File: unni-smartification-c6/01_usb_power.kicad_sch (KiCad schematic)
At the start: 36 parts, among them J1 USB-C (replacement daughterbo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, J2 Li-Ion 1S JST-PH, J4 UNNI DC / battery input - AC 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, Q1 AO3401A, Q2 AO3401A, Q3 AO3400A, Q4 AO3400A, U1 MCP73831T-2ACI/OT, U2 TPS63031DSK, U3 TPS613222ADBZ (5V)

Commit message: trying routing the usb-pcb
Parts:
- added U4: USBLC6-2SC6, Package_TO_SOT_SMD:SOT-23-6, symbol Power_Protection:USBLC6-2SC6
- D1, D3, D4: footprint Diode_SMD:D_SMA -> Diode_SMD:D_SMA_Handsoldering
- Q1, Q2, Q3, Q4, U3: footprint Package_TO_SOT_SMD:SOT-23 -> Package_TO_SOT_SMD:SOT-23_Handsoldering
- U1: footprint Package_TO_SOT_SMD:SOT-23-5 -> Package_TO_SOT_SMD:SOT-23-5_HandSoldering
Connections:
- net +BATT: now also J2.2 (Pin_2); no longer J2.1 (Pin_1)
- net GND: now also J2.1 (Pin_1), U4.2 (GND); no longer J2.2 (Pin_2)
- net USB_RAW_N: now also U4.6 (I/O1); no longer J1.A7 (DN1), J1.B7 (DN2)
- net USB_RAW_P: now also U4.4 (I/O2); no longer J1.A6 (DP1), J1.B6 (DP2)
- net VBUS: now also U4.5 (VBUS)
- new net USB_N: J1.A7 (DN1), J1.B7 (DN2), U4.1 (I/O1)
- new net USB_P: J1.A6 (DP1), J1.B6 (DP2), U4.3 (I/O2)

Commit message: add usb-esp and finalize usb-pcb
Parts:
- added C14: 100n, Capacitor_SMD:C_0603_1608Metric_Pad1.08x0.95mm_HandSolder, symbol Device:C
- L1: value 1.5uH -> 2.2uH
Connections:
- net GND: now also C14.2
- net VBUS: now also C14.1
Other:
- moved on the sheet: R1
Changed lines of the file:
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@@
 	)
 	(junction
+		(at 66.04 46.99)
+		(diameter 0)
+		(color 0 0 0 0)
+	)
+	(junction
 		(at 66.04 53.34)
 		(diameter 0)
@@
 	)
 	(junction
+		(at 66.04 30.48)
+		(diameter 0)
+		(color 0 0 0 0)
+	)
+	(junction
 		(at 49.53 73.66)
 		(diameter 0)
@@
 	(wire
 		(pts
+			(xy 66.04 30.48) (xy 90.17 30.48)
+		)
+		(stroke
+			(width 0)
+			(type default)
+		)
+	)
+	(wire
+		(pts
 			(xy 39.37 172.72) (xy 39.37 193.04)
 		)
@@
 	(wire
 		(pts
-			(xy 45.72 53.34) (xy 50.8 53.34)
+			(xy 45.72 53.34) (xy 52.07 53.34)
 		)
 		(stroke
@@
 	(wire
 		(pts
+			(xy 66.04 46.99) (xy 66.04 53.34)
+		)
+		(stroke
+			(width 0)
+			(type default)
+		)
+	)
+	(wire
+		(pts
 			(xy 137.16 31.75) (xy 137.16 30.48)
 		)
@@
 	(wire
 		(pts
+			(xy 66.04 46.99) (xy 90.17 46.99)
+		)
+		(stroke
+			(width 0)
+			(type default)
+		)
+	)
+	(wire
+		(pts
 			(xy 45.72 33.02) (xy 50.8 33.02)
 		)
@@
 	(wire
 		(pts
+			(xy 90.17 30.48) (xy 90.17 34.29)
+		)
+		(stroke
+			(width 0)
+			(type default)
+		)
+	)
+	(wire
+		(pts
 			(xy 133.35 189.23) (xy 133.35 191.77)
 		)
@@
 	(wire
 		(pts
-			(xy 66.04 45.72) (xy 66.04 53.34)
+			(xy 66.04 45.72) (xy 66.04 46.99)
 		)
 		(stroke
@@
 	(wire
 		(pts
-			(xy 58.42 53.34) (xy 66.04 53.34)
+			(xy 59.69 53.34) (xy 66.04 53.34)
 		)
 		(stroke
@@
 	(wire
 		(pts
+			(xy 90.17 41.91) (xy 90.17 46.99)
+		)
+		(stroke
+			(width 0)
+			(type default)
+		)
+	)
+	(wire
+		(pts
 			(xy 123.19 39.37) (xy 123.19 54.61)
 		)
@@
 	(symbol
 		(lib_id "Device:R")
-		(at 54.61 53.34 90)
+		(at 55.88 53.34 90)
 		(unit 1)
 		(body_style 1)
@@
 		(fields_autoplaced yes)
 		(property "Reference" "R1"
-			(at 54.61 46.99 90)
+			(at 55.88 46.99 90)
 			(show_name no)
 			(do_not_autoplace no)
@@
 		)
 		(property "Value" "5.1k"
-			(at 54.61 49.53 90)
+			(at 55.88 49.53 90)
 			(show_name no)
 			(do_not_autoplace no)
@@
 		)
 		(property "Footprint" "Resistor_SMD:R_0805_2012Metric_Pad1.20x1.40mm_HandSolder"
-			(at 54.61 53.34 0)
+			(at 55.88 53.34 0)
 			(hide yes)
 			(show_name no)
@@
 		)
 		(property "Datasheet" ""
-			(at 54.61 53.34 0)
+			(at 55.88 53.34 0)
 			(hide yes)
 			(show_name no)
@@
 		)
 		(property "Description" ""
-			(at 54.61 53.34 0)
+			(at 55.88 53.34 0)
 			(hide yes)
 			(show_name no)
@@
 			)
 		)
-		(property "Value" "1.5uH"
+		(property "Value" "2.2uH"
 			(at 186.69 130.81 0)
 			(show_name no)
@@
 	)
 	(symbol
+		(lib_id "Device:C")
+		(at 90.17 38.1 0)
+		(unit 1)
+		(body_style 1)
+		(exclude_from_sim yes)
+		(in_bom yes)
+		(on_board yes)
+		(in_pos_files yes)
+		(dnp no)
+		(fields_autoplaced yes)
+		(property "Reference" "C14"
+			(at 93.98 36.8299 0)
+			(show_name no)
+			(do_not_autoplace no)
+			(effects
+				(font
+					(size 1.27 1.27)
+				)
+				(justify left)
+			)
+		)
+		(property "Value" "100n"
+			(at 93.98 39.3699 0)
+			(show_name no)
+			(do_not_autoplace no)
+			(effects
+				(font
+					(size 1.27 1.27)
+				)
+				(justify left)
+			)
+		)
+		(property "Footprint" "Capacitor_SMD:C_0603_1608Metric_Pad1.08x0.95mm_HandSolder"
+			(at 91.1352 41.91 0)
+			(hide yes)
+			(show_name no)
+			(do_not_autoplace no)
+			(effects
+				(font
+					(size 1.27 1.27)
+				)
+			)
+		)
+		(property "Datasheet" ""
+			(at 90.17 38.1 0)
+			(hide yes)
+			(show_name no)
+			(do_not_autoplace no)
+			(effects
+				(font
+					(size 1.27 1.27)
+				)
+			)
+		)
+		(property "Description" "Unpolarized capacitor"
+			(at 90.17 38.1 0)
+			(hide yes)
+			(show_name no)
+			(do_not_autoplace no)
+			(effects
+				(font
+					(size 1.27 1.27)
+				)
+			)
+		)
+		(pin "1"
+		)
+		(pin "2"
+		)
+		(instances
+			(project "unni-smartification-c6"
+				(path "/15fd0edf-be3e-44ec-8dd6-6b1cf69b7c51/c2ff28aa-a0f2-4a89-9a60-62d08b111b12"
+					(reference "C14")
+					(unit 1)
+				)
+			)
+		)
+	)
+	(symbol
 		(lib_id "power:+5V")
 		(at 227.33 168.91 0)
@@
 		(unit 1)
 		(body_style 1)
-		(exclude_from_sim no)
+		(exclude_from_sim yes)
 		(in_bom yes)
 		(on_board yes)
@@
 		)
 		(property "Value" "VBUS"
-			(at 50.8 22.86 0)
+			(at 53.34 26.67 0)
 			(show_name no)
 			(do_not_autoplace no)
@@
 					(size 1 1)
 				)
+				(justify left)
 			)
 		)
@@
 		)
 		(property "Value" "GND"
-			(at 66.04 88.9 0)
+			(at 68.58 85.09 0)
 			(show_name no)
 			(do_not_autoplace no)
@@
 					(size 1 1)
 				)
+				(justify left)
 			)
 		)
@@
 		(in_pos_files yes)
 		(dnp no)
+		(fields_autoplaced yes)
 		(property "Reference" "J2"
-			(at 34.29 110.49 0)
+			(at 34.29 95.25 0)
 			(show_name no)
 			(do_not_autoplace no)
@@
 		)
 		(property "Value" "Li-Ion 1S JST-PH"
-			(at 34.29 107.95 0)
+			(at 34.29 97.79 0)
 			(show_name no)
 			(do_not_autoplace no)

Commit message: move some power stuff to esp board, update some footprints
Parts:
- removed C1, C2: 4.7uF, Capacitor_SMD:C_0805_2012Metric_Pad1.18x1.45mm_HandSolder, symbol Device:C
- removed C3, C5, C6: 10uF, Capacitor_SMD:C_0805_2012Metric_Pad1.18x1.45mm_HandSolder, symbol Device:C
- removed C4: 100nF, Capacitor_SMD:C_0603_1608Metric_Pad1.08x0.95mm_HandSolder, symbol Device:C
- removed D1: SS14, Diode_SMD:D_SMA_Handsoldering, symbol Diode:SB120
- removed J2: Li-Ion 1S JST-PH, Connector_JST:JST_PH_S2B-PH-SM4-TB_1x02-1MP_P2.00mm_Horizontal, symbol Connector_Generic:Conn_01x02
- removed L1: 2.2uH, Inductor_SMD:L_TDK_NLV32_3.2x2.5mm, symbol Device:L
- removed Q1: AO3401A, Package_TO_SOT_SMD:SOT-23_Handsoldering, symbol Transistor_FET:TP0610T
- removed R11: 150k, Resistor_SMD:R_0805_2012Metric_Pad1.20x1.40mm_HandSolder, symbol Device:R
- removed R12: 220k, Resistor_SMD:R_0805_2012Metric_Pad1.20x1.40mm_HandSolder, symbol Device:R
- removed R3: 3.3k, Resistor_SMD:R_0805_2012Metric_Pad1.20x1.40mm_HandSolder, symbol Device:R
- removed R5: 100k, Resistor_SMD:R_0805_2012Metric_Pad1.20x1.40mm_HandSolder, symbol Device:R
- removed R6: 1M, Resistor_SMD:R_0805_2012Metric_Pad1.20x1.40mm_HandSolder, symbol Device:R
- removed U1: MCP73831T-2ACI/OT, Package_TO_SOT_SMD:SOT-23-5_HandSoldering, symbol Battery_Management:MCP73831-2-OT
- removed U2: TPS63031DSK, Package_SON:WSON-10-1EP_2.5x2.5mm_P0.5mm_EP1.2x2mm, symbol Regulator_Switching:TPS63030DSK
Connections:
- net GND: now also J4.2 (Pin_2); no longer J4.3 (Pin_3)
- net UNNI_AC: now also J4.3 (Pin_3); no longer J4.2 (Pin_2)
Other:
- note removed: "RPROG 3.3k = ~303 mA nominal charge current"
- moved on the sheet: D3, D4

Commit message: re-do ESP PCB
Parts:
- added J3: Conn_01x01, Connector_Wire:SolderWire-0.5sqmm_1x01_D0.9mm_OD2.1mm, symbol Connector_Generic:Conn_01x01
- added J5, J6, J7, J8, J9: Conn_01x01, Connector_Wire:SolderWire-0.1sqmm_1x01_D0.4mm_OD1mm, symbol Connector_Generic:Conn_01x01
- L2: footprint Inductor_SMD:L_TDK_NLV32_3.2x2.5mm -> Unni_Inductor:L_Murata_DFE322520FD_3.2x2.5mm_HandSolder
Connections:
- net BOOST_CMD: now also J5.1 (Pin_1)
- net USB_N renamed USBPort_N
- net USB_P renamed USBPort_P
- net USB_RAW_N renamed CONN_USB_N
- net CONN_USB_N: now also J9.1 (Pin_1)
- net USB_RAW_P renamed CONN_USB_P
- net CONN_USB_P: now also J8.1 (Pin_1)
- new net CONN_+BATT: J7.1 (Pin_1)
- new net CONN_GND: J3.1 (Pin_1)
- new net CONN_VBUS: J6.1 (Pin_1)

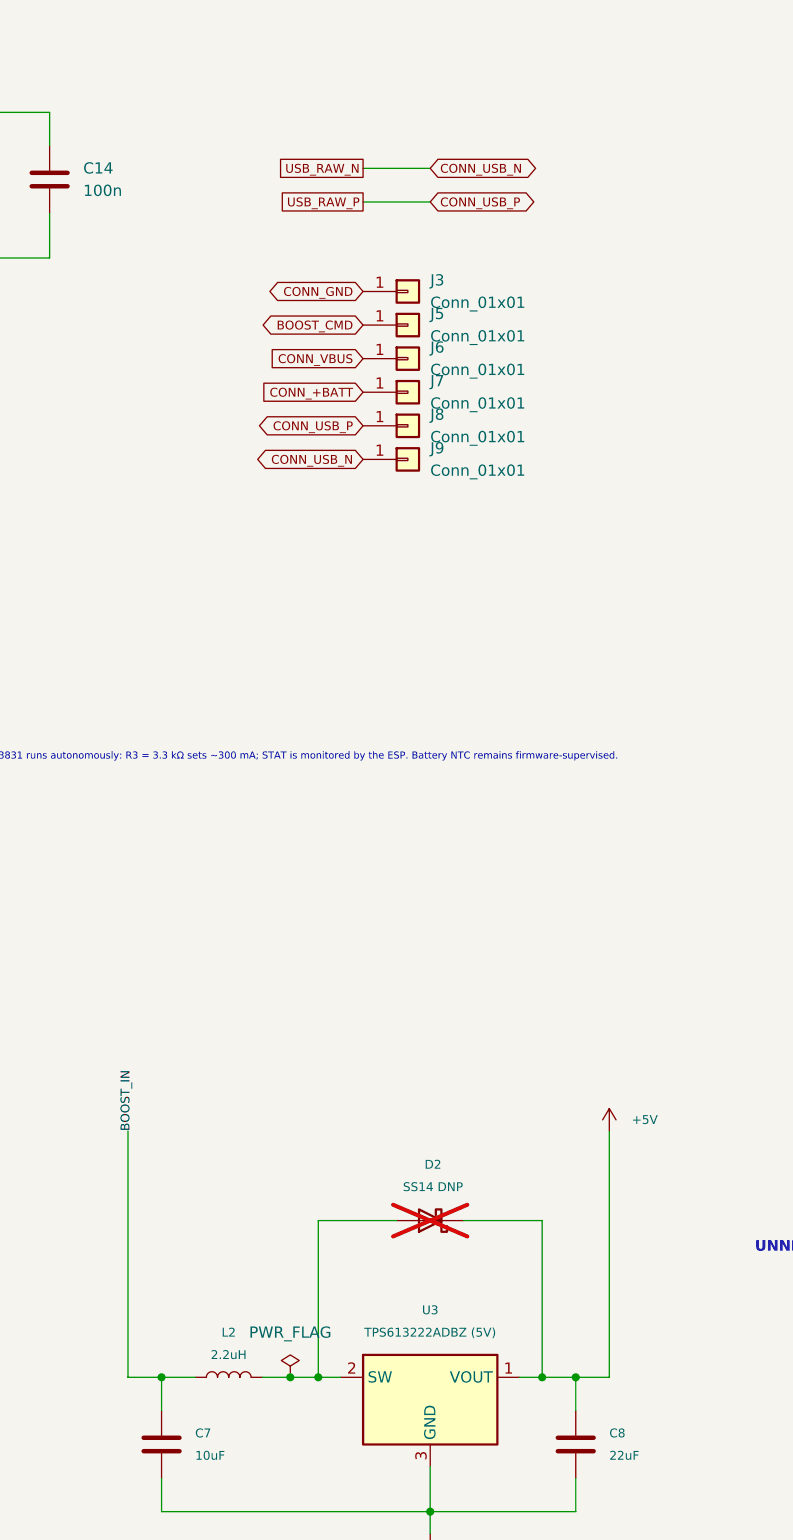
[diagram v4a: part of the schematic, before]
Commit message: Clean up power nets and routing rules
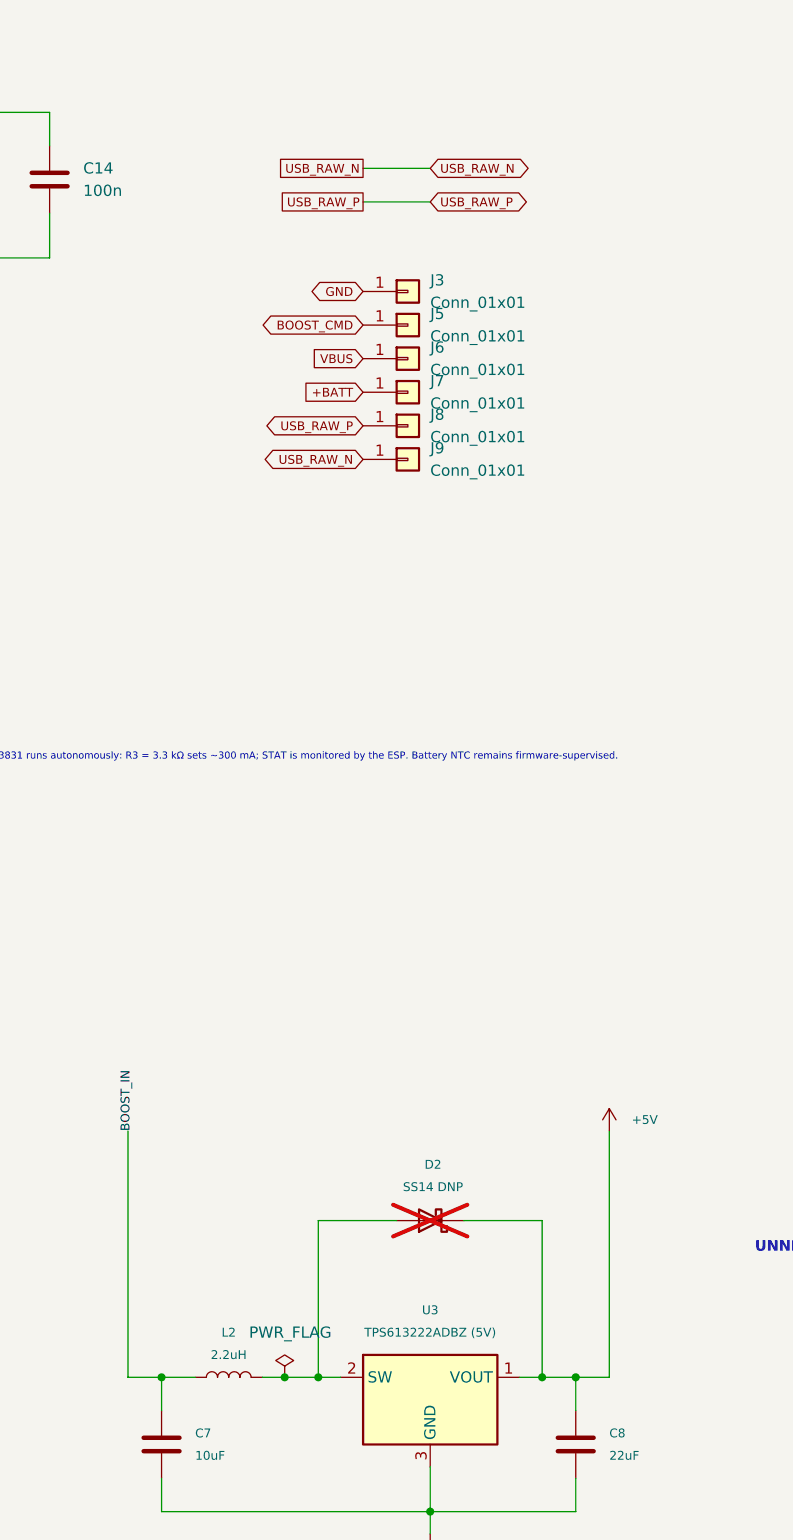
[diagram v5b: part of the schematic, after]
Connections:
- net CONN_+BATT is gone; now on net +BATT: J7.1 (Pin_1)
- net CONN_GND is gone; now on net GND: J3.1 (Pin_1)
- net CONN_VBUS is gone; now on net VBUS: J6.1 (Pin_1)
- net CONN_USB_N renamed USB_RAW_N
- net CONN_USB_P renamed USB_RAW_P
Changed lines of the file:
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@@
 	)
 	(junction
-		(at 117.475 173.99)
+		(at 116.84 173.99)
 		(diameter 0)
 		(color 0 0 0 0)
@@
 	(wire
 		(pts
-			(xy 117.475 173.99) (xy 120.65 173.99)
+			(xy 116.84 173.99) (xy 120.65 173.99)
 		)
 		(stroke
@@
 	(wire
 		(pts
-			(xy 114.3 173.99) (xy 117.475 173.99)
+			(xy 114.3 173.99) (xy 116.84 173.99)
 		)
 		(stroke
@@
 		)
 	)
-	(global_label "CONN_USB_P"
+	(global_label "USB_RAW_P"
 		(shape bidirectional)
 		(at 125.73 66.04 180)
@@
 		)
 	)
-	(global_label "CONN_+BATT"
+	(global_label "+BATT"
 		(shape input)
 		(at 125.73 62.23 180)
@@
 		)
 	)
-	(global_label "CONN_USB_P"
+	(global_label "USB_RAW_P"
 		(shape bidirectional)
 		(at 133.35 40.64 0)
@@
 		)
 	)
-	(global_label "CONN_GND"
+	(global_label "GND"
 		(shape bidirectional)
 		(at 125.73 50.8 180)
@@
 		)
 	)
-	(global_label "CONN_USB_N"
+	(global_label "USB_RAW_N"
 		(shape bidirectional)
 		(at 133.35 36.83 0)
@@
 		)
 	)
-	(global_label "CONN_USB_N"
+	(global_label "USB_RAW_N"
 		(shape bidirectional)
 		(at 125.73 69.85 180)
@@
 		)
 	)
-	(global_label "CONN_VBUS"
+	(global_label "VBUS"
 		(shape input)
 		(at 125.73 58.42 180)
@@
 		(unit 1)
 		(body_style 1)
-		(exclude_from_sim no)
+		(exclude_from_sim yes)
 		(in_bom yes)
 		(on_board yes)
@@
 		(unit 1)
 		(body_style 1)
-		(exclude_from_sim no)
+		(exclude_from_sim yes)
 		(in_bom yes)
 		(on_board yes)
@@
 	(symbol
 		(lib_id "power:PWR_FLAG")
-		(at 117.475 173.99 0)
+		(at 116.84 173.99 0)
 		(unit 1)
 		(body_style 1)
@@
 		)
 		(property "Footprint" ""
-			(at 117.475 173.99 0)
+			(at 116.84 173.99 0)
 			(hide yes)
 			(show_name no)
@@
 		)
 		(property "Datasheet" ""
-			(at 117.475 173.99 0)
+			(at 116.84 173.99 0)
 			(hide yes)
 			(show_name no)
@@
 		)
 		(property "Description" "Special symbol for telling ERC where power comes from"
-			(at 117.475 173.99 0)
+			(at 116.84 173.99 0)
 			(hide yes)
 			(show_name no)
@@
 		(unit 1)
 		(body_style 1)
-		(exclude_from_sim no)
+		(exclude_from_sim yes)
 		(in_bom yes)
 		(on_board yes)
@@
 		(unit 1)
 		(body_style 1)
-		(exclude_from_sim no)
+		(exclude_from_sim yes)
 		(in_bom yes)
 		(on_board yes)
@@
 		(unit 1)
 		(body_style 1)
-		(exclude_from_sim no)
+		(exclude_from_sim yes)
 		(in_bom yes)
 		(on_board yes)
@@
 		(unit 1)
 		(body_style 1)
-		(exclude_from_sim no)
+		(exclude_from_sim yes)
 		(in_bom yes)
 		(on_board yes)

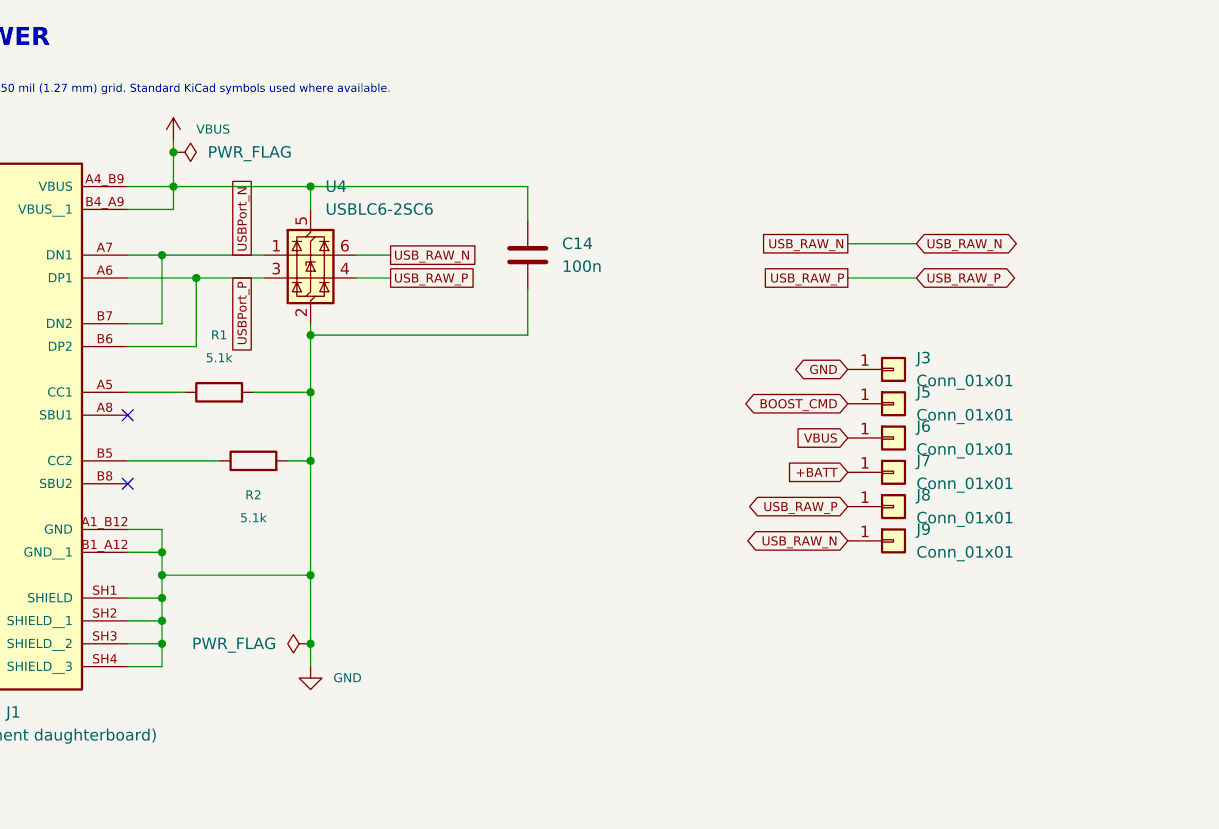
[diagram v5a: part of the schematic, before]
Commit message: new tvs diode, final fiddlings
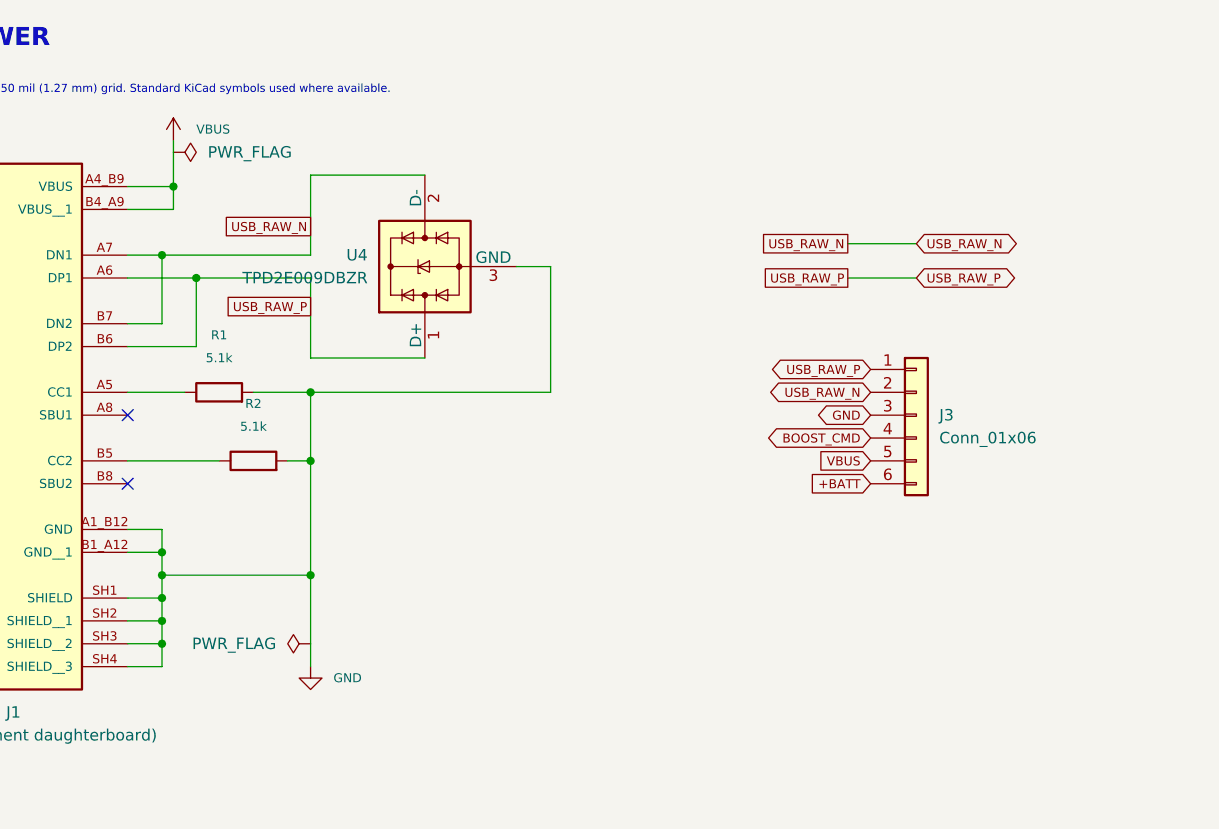
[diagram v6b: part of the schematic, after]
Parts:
- removed C14: 100n, Capacitor_SMD:C_0603_1608Metric_Pad1.08x0.95mm_HandSolder, symbol Device:C
- removed J3: Conn_01x01, Connector_Wire:SolderWire-0.5sqmm_1x01_D0.9mm_OD2.1mm, symbol Connector_Generic:Conn_01x01
- removed J5, J6, J7, J8, J9: Conn_01x01, Connector_Wire:SolderWire-0.1sqmm_1x01_D0.4mm_OD1mm, symbol Connector_Generic:Conn_01x01
- removed U4: USBLC6-2SC6, Package_TO_SOT_SMD:SOT-23-6, symbol Power_Protection:USBLC6-2SC6
- added J3: Conn_01x06, Connector_JST:JST_PH_B6B-PH-K_1x06_P2.00mm_Vertical, symbol Connector_Generic:Conn_01x06
- added U4: TPD2E009DBZR, Package_TO_SOT_SMD:SOT-23_Handsoldering, symbol Power_Protection:TPD2EUSB30
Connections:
- net USBPort_N is gone; now on net USB_RAW_N: J1.A7 (DN1), J1.B7 (DN2)
- net USBPort_P is gone; now on net USB_RAW_P: J1.A6 (DP1), J1.B6 (DP2)
- net +BATT: now also J3.6 (Pin_6)
- net BOOST_CMD: now also J3.4 (Pin_4)
- net GND: now also J3.3 (Pin_3), U4.3 (GND)
- net USB_RAW_N: now also J3.2 (Pin_2), U4.2 (D-)
- net USB_RAW_P: now also J3.1 (Pin_1), U4.1 (D+)
- net VBUS: now also J3.5 (Pin_5)
